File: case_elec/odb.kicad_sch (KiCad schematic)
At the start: 1 part, among them U2 Teensy3.5

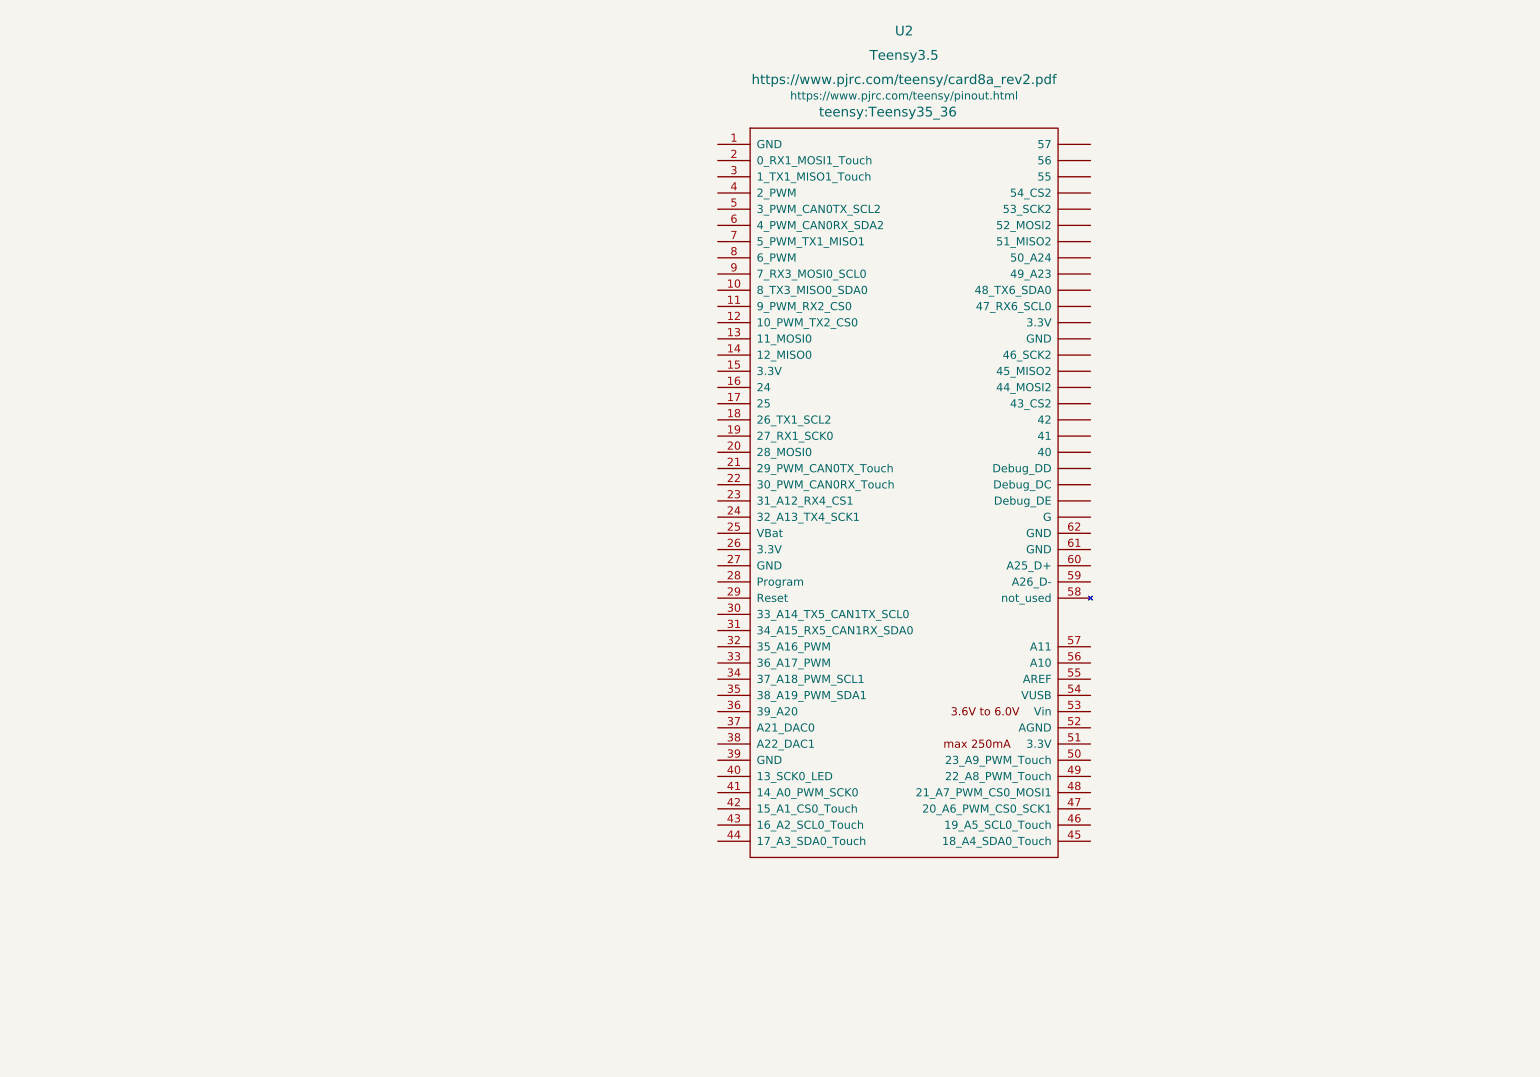
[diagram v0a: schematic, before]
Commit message: Ajout des capteurs
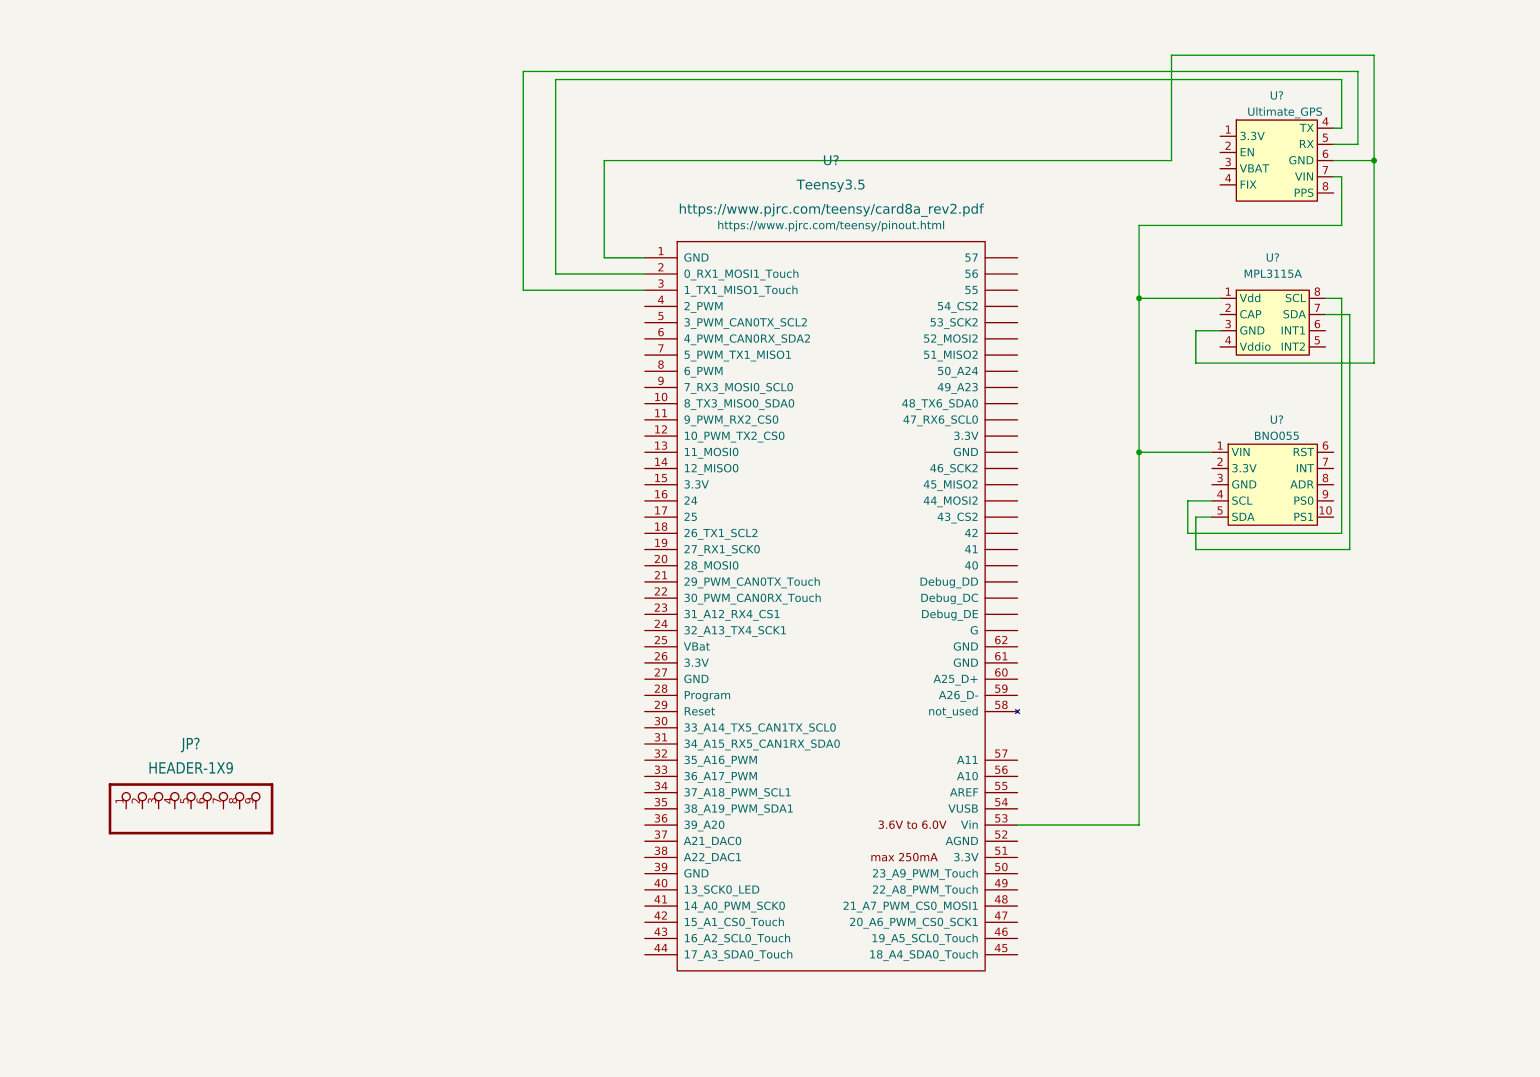
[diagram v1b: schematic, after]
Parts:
- removed U2: Teensy3.5, teensy:Teensy35_36, symbol teensy:Teensy3.5
- added JP?: HEADER-1X9, PCB_case_elec:1X09_OVAL, symbol PCB_case_elec-eagle-import:HEADER-1X9
- added U?: MPL3115A, symbol Adafruit_sensors:MPL3115A
- added U?: Teensy3.5, symbol Teensy:Teensy3.5
- added U?: Ultimate_GPS, symbol Adafruit_sensors:Ultimate_GPS
- added U?: BNO055, symbol Adafruit_sensors:BNO055
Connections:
- new net: U?.1 (VIN), U?.1 (Vdd), U?.53 (Vin), U?.7 (VIN)
- new net: U?.1 (GND), U?.3 (GND), U?.6 (GND)
- new net: U?.5 (SDA), U?.7 (SDA)
- new net: U?.4 (SCL), U?.8 (SCL)
- new net: U?.2 (0_RX1_MOSI1_Touch), U?.4 (TX)
- new net: U?.3 (1_TX1_MISO1_Touch), U?.5 (RX)
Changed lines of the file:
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@@
     (comment 3 "<mohamed-iadh.bani@top-aero.com> <theo.tugaye@top-aero.com>")
   )
-  (symbol (lib_id "teensy:Teensy3.5") (at 152.4 92.71 0) (unit 1)
-    (in_bom yes) (on_board yes)
-    (property "Reference" "U2" (id 0) (at 152.4 20.32 0)
+  (junction (at 226.06 40.64) (diameter 0) (color 0 0 0 0)
+  )
+  (junction (at 189.23 62.23) (diameter 0) (color 0 0 0 0)
+  )
+  (junction (at 189.23 86.36) (diameter 0) (color 0 0 0 0)
+  )
+  (wire (pts (xy 222.25 101.6) (xy 198.12 101.6))
+    (stroke (width 0) (type default) (color 0 0 0 0))
+  )
+  (wire (pts (xy 111.76 58.42) (xy 97.79 58.42))
+    (stroke (width 0) (type default) (color 0 0 0 0))
+  )
+  (wire (pts (xy 196.85 99.06) (xy 196.85 93.98))
+    (stroke (width 0) (type default) (color 0 0 0 0))
+  )
+  (wire (pts (xy 189.23 50.8) (xy 189.23 62.23))
+    (stroke (width 0) (type default) (color 0 0 0 0))
+  )
+  (wire (pts (xy 189.23 86.36) (xy 189.23 144.78))
+    (stroke (width 0) (type default) (color 0 0 0 0))
+  )
+  (wire (pts (xy 220.98 43.18) (xy 220.98 50.8))
+    (stroke (width 0) (type default) (color 0 0 0 0))
+  )
+  (wire (pts (xy 223.52 26.67) (xy 223.52 38.1))
+    (stroke (width 0) (type default) (color 0 0 0 0))
+  )
+  (wire (pts (xy 198.12 67.31) (xy 198.12 72.39))
+    (stroke (width 0) (type default) (color 0 0 0 0))
+  )
+  (wire (pts (xy 201.93 67.31) (xy 198.12 67.31))
+    (stroke (width 0) (type default) (color 0 0 0 0))
+  )
+  (wire (pts (xy 201.93 62.23) (xy 189.23 62.23))
+    (stroke (width 0) (type default) (color 0 0 0 0))
+  )
+  (wire (pts (xy 92.71 60.96) (xy 92.71 26.67))
+    (stroke (width 0) (type default) (color 0 0 0 0))
+  )
+  (wire (pts (xy 218.44 62.23) (xy 220.98 62.23))
+    (stroke (width 0) (type default) (color 0 0 0 0))
+  )
+  (wire (pts (xy 92.71 26.67) (xy 223.52 26.67))
+    (stroke (width 0) (type default) (color 0 0 0 0))
+  )
+  (wire (pts (xy 220.98 99.06) (xy 196.85 99.06))
+    (stroke (width 0) (type default) (color 0 0 0 0))
+  )
+  (wire (pts (xy 198.12 72.39) (xy 226.06 72.39))
+    (stroke (width 0) (type default) (color 0 0 0 0))
+  )
+  (wire (pts (xy 194.31 40.64) (xy 194.31 24.13))
+    (stroke (width 0) (type default) (color 0 0 0 0))
+  )
+  (wire (pts (xy 219.71 43.18) (xy 220.98 43.18))
+    (stroke (width 0) (type default) (color 0 0 0 0))
+  )
+  (wire (pts (xy 196.85 93.98) (xy 200.66 93.98))
+    (stroke (width 0) (type default) (color 0 0 0 0))
+  )
+  (wire (pts (xy 189.23 86.36) (xy 200.66 86.36))
+    (stroke (width 0) (type default) (color 0 0 0 0))
+  )
+  (wire (pts (xy 219.71 38.1) (xy 223.52 38.1))
+    (stroke (width 0) (type default) (color 0 0 0 0))
+  )
+  (wire (pts (xy 194.31 40.64) (xy 105.41 40.64))
+    (stroke (width 0) (type default) (color 0 0 0 0))
+  )
+  (wire (pts (xy 97.79 27.94) (xy 220.98 27.94))
+    (stroke (width 0) (type default) (color 0 0 0 0))
+  )
+  (wire (pts (xy 220.98 27.94) (xy 220.98 35.56))
+    (stroke (width 0) (type default) (color 0 0 0 0))
+  )
+  (wire (pts (xy 198.12 101.6) (xy 198.12 96.52))
+    (stroke (width 0) (type default) (color 0 0 0 0))
+  )
+  (wire (pts (xy 189.23 62.23) (xy 189.23 86.36))
+    (stroke (width 0) (type default) (color 0 0 0 0))
+  )
+  (wire (pts (xy 105.41 55.88) (xy 111.76 55.88))
+    (stroke (width 0) (type default) (color 0 0 0 0))
+  )
+  (wire (pts (xy 219.71 35.56) (xy 220.98 35.56))
+    (stroke (width 0) (type default) (color 0 0 0 0))
+  )
+  (wire (pts (xy 226.06 24.13) (xy 226.06 40.64))
+    (stroke (width 0) (type default) (color 0 0 0 0))
+  )
+  (wire (pts (xy 219.71 40.64) (xy 226.06 40.64))
+    (stroke (width 0) (type default) (color 0 0 0 0))
+  )
+  (wire (pts (xy 111.76 60.96) (xy 92.71 60.96))
+    (stroke (width 0) (type default) (color 0 0 0 0))
+  )
+  (wire (pts (xy 222.25 64.77) (xy 222.25 101.6))
+    (stroke (width 0) (type default) (color 0 0 0 0))
+  )
+  (wire (pts (xy 170.18 144.78) (xy 189.23 144.78))
+    (stroke (width 0) (type default) (color 0 0 0 0))
+  )
+  (wire (pts (xy 226.06 40.64) (xy 226.06 72.39))
+    (stroke (width 0) (type default) (color 0 0 0 0))
+  )
+  (wire (pts (xy 220.98 50.8) (xy 189.23 50.8))
+    (stroke (width 0) (type default) (color 0 0 0 0))
+  )
+  (wire (pts (xy 105.41 40.64) (xy 105.41 55.88))
+    (stroke (width 0) (type default) (color 0 0 0 0))
+  )
+  (wire (pts (xy 218.44 64.77) (xy 222.25 64.77))
+    (stroke (width 0) (type default) (color 0 0 0 0))
+  )
+  (wire (pts (xy 194.31 24.13) (xy 226.06 24.13))
+    (stroke (width 0) (type default) (color 0 0 0 0))
+  )
+  (wire (pts (xy 220.98 62.23) (xy 220.98 99.06))
+    (stroke (width 0) (type default) (color 0 0 0 0))
+  )
+  (wire (pts (xy 198.12 96.52) (xy 200.66 96.52))
+    (stroke (width 0) (type default) (color 0 0 0 0))
+  )
+  (wire (pts (xy 97.79 58.42) (xy 97.79 27.94))
+    (stroke (width 0) (type default) (color 0 0 0 0))
+  )
+  (symbol (lib_id "Adafruit_sensors:MPL3115A") (at 214.63 66.04 0) (unit 1)
+    (in_bom yes) (on_board yes) (fields_autoplaced)
+    (property "Reference" "U?" (id 0) (at 210.185 55.88 0))
+    (property "Value" "MPL3115A" (id 1) (at 210.185 58.42 0))
+    (property "Footprint" "" (id 2) (at 218.44 66.04 0)
+      (effects (font (size 1.27 1.27)) hide)
+    )
+    (property "Datasheet" "" (id 3) (at 218.44 66.04 0)
+      (effects (font (size 1.27 1.27)) hide)
+    )
+    (pin "1")
+    (pin "2")
+    (pin "3")
+    (pin "4")
+    (pin "5")
+    (pin "6")
+    (pin "7")
+    (pin "8")
+  )
+  (symbol (lib_id "Teensy:Teensy3.5") (at 140.97 110.49 0) (unit 1)
+    (in_bom yes) (on_board yes) (fields_autoplaced)
+    (property "Reference" "U?" (id 0) (at 140.97 40.64 0)
       (effects (font (size 1.524 1.524)))
     )
-    (property "Value" "Teensy3.5" (id 1) (at 152.4 24.13 0)
+    (property "Value" "Teensy3.5" (id 1) (at 140.97 44.45 0)
       (effects (font (size 1.524 1.524)))
     )
-    (property "Footprint" "teensy:Teensy35_36" (id 2) (at 149.86 33.02 0)
+    (property "Footprint" "" (id 2) (at 138.43 53.34 0)
       (effects (font (size 1.524 1.524)))
     )
-    (property "Datasheet" "https://www.pjrc.com/teensy/card8a_rev2.pdf" (id 3) (at 152.4 27.94 0)
+    (property "Datasheet" "https://www.pjrc.com/teensy/card8a_rev2.pdf" (id 3) (at 140.97 48.26 0)
       (effects (font (size 1.524 1.524)))
     )
-    (property "Pinouts" "https://www.pjrc.com/teensy/pinout.html" (id 4) (at 152.4 30.48 0))
+    (property "Pinouts" "https://www.pjrc.com/teensy/pinout.html" (id 4) (at 140.97 50.8 0))
     (pin "1")
     (pin "10")
@@
     (pin "~")
   )
+  (symbol (lib_id "PCB_case_elec-eagle-import:HEADER-1X9") (at 40.64 139.7 90) (unit 1)
+    (in_bom yes) (on_board yes) (fields_autoplaced)
+    (property "Reference" "JP?" (id 0) (at 40.64 132.08 90)
+      (effects (font (size 1.778 1.5113)))
+    )
+    (property "Value" "HEADER-1X9" (id 1) (at 40.64 135.89 90)
+      (effects (font (size 1.778 1.5113)))
+    )
+    (property "Footprint" "PCB_case_elec:1X09_OVAL" (id 2) (at 40.64 139.7 0)
+      (effects (font (size 1.27 1.27)) hide)
+    )
+    (property "Datasheet" "" (id 3) (at 40.64 139.7 0)
+      (effects (font (size 1.27 1.27)) hide)
+    )
+    (pin "1")
+    (pin "2")
+    (pin "3")
+    (pin "4")
+    (pin "5")
+    (pin "6")
+    (pin "7")
+    (pin "8")
+    (pin "9")
+  )
+  (symbol (lib_id "Adafruit_sensors:Ultimate_GPS") (at 210.82 41.91 0) (unit 1)
+    (in_bom yes) (on_board yes)
+    (property "Reference" "U?" (id 0) (at 210.82 30.48 0))
+    (property "Value" "Ultimate_GPS" (id 1) (at 212.09 33.02 0))
+    (property "Footprint" "" (id 2) (at 203.835 34.29 0)
+      (effects (font (size 1.27 1.27)) hide)
+    )
+    (property "Datasheet" "" (id 3) (at 203.835 34.29 0)
+      (effects (font (size 1.27 1.27)) hide)
+    )
+    (pin "1")
+    (pin "2")
+    (pin "3")
+    (pin "4")
+    (pin "4")
+    (pin "5")
+    (pin "6")
+    (pin "7")
+    (pin "8")
+  )
+  (symbol (lib_name "BNO055_1") (lib_id "Adafruit_sensors:BNO055") (at 210.82 91.44 0) (unit 1)
+    (in_bom yes) (on_board yes)
+    (property "Reference" "U?" (id 0) (at 210.82 81.28 0))
+    (property "Value" "BNO055" (id 1) (at 210.82 83.82 0))
+    (property "Footprint" "" (id 2) (at 203.2 86.36 0)
+      (effects (font (size 1.27 1.27)) hide)
+    )
+    (property "Datasheet" "" (id 3) (at 203.2 86.36 0)
+      (effects (font (size 1.27 1.27)) hide)
+    )
+    (pin "1")
+    (pin "10")
+    (pin "2")
+    (pin "3")
+    (pin "4")
+    (pin "5")
+    (pin "6")
+    (pin "7")
+    (pin "8")
+    (pin "9")
+  )
   (sheet_instances
     (path "/" (page "1"))
   )
   (symbol_instances
-    (path "/aea79e9c-cd11-42c5-a914-4323a1da44dd"
-      (reference "U2") (unit 1) (value "Teensy3.5") (footprint "teensy:Teensy35_36")
-    )
-  )
+    (path "/74241264-0098-4d88-8365-65d717f7e09d"
+      (reference "JP?") (unit 1) (value "HEADER-1X9") (footprint "PCB_case_elec:1X09_OVAL")
+    )
+    (path "/4324021c-adf2-48f1-8a00-7ea1c3478302"
+      (reference "U?") (unit 1) (value "MPL3115A") (footprint "")
+    )
+    (path "/6dbf9b0b-d170-42c2-945f-d4ad0c4354aa"
+      (reference "U?") (unit 1) (value "Teensy3.5") (footprint "")
+    )
+    (path "/857fdb2b-599c-415c-9c78-a5968f20db3d"
+      (reference "U?") (unit 1) (value "Ultimate_GPS") (footprint "")
+    )
+    (path "/8ab76ae2-3e2d-49e7-a48d-245f963932e6"
+      (reference "U?") (unit 1) (value "BNO055") (footprint "")
+    )
+  )
